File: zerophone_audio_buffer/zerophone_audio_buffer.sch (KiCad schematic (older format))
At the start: 7 parts, among them P1 CONN_01X03, P2 CONN_01X04, U1 LM1117-2.5, U2 NC7WZ16

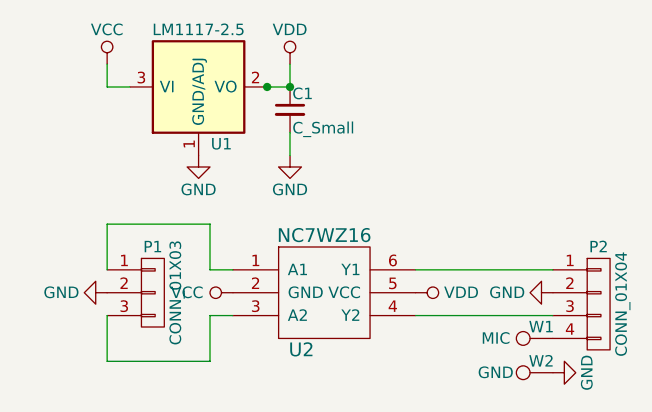
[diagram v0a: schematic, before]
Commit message: Corrected buffer pinout; changed power symbols
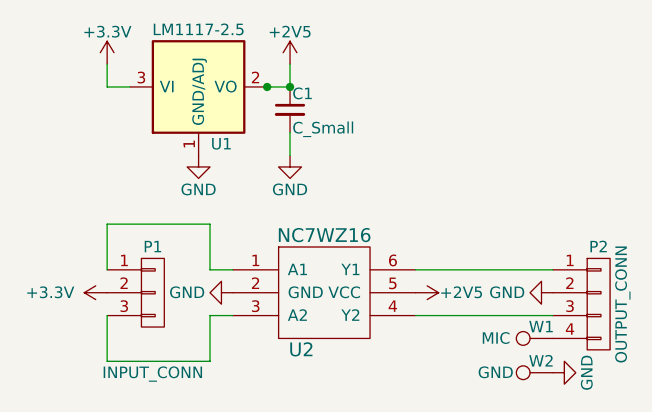
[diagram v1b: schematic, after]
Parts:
- P1: value CONN_01X03 -> INPUT_CONN
- P2: value CONN_01X04 -> OUTPUT_CONN
- W1, W2: footprint (none) -> Measurement_Points:Measurement_Point_Round-SMD-Pad_Small
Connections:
- net GND: now also U2.2 (GND); no longer P1.2 (P2)
- net VCC renamed +3V3
- net +3V3: now also P1.2 (P2); no longer U2.2 (GND)
- net VDD renamed +2V5
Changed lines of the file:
@@
 L GND #PWR01
 U 1 1 58BC7F11
-P 4850 2600
-F 0 "#PWR01" H 4850 2350 50  0001 C CNN
-F 1 "GND" V 4850 2400 50  0000 C CNN
-F 2 "" H 4850 2600 50  0000 C CNN
-F 3 "" H 4850 2600 50  0000 C CNN
-	1    4850 2600
-	0    1    1    0
-$EndComp
-$Comp
-L VDD #PWR02
-U 1 1 58BC7F41
-P 3700 1600
-F 0 "#PWR02" H 3700 1450 50  0001 C CNN
-F 1 "VDD" H 3700 1750 50  0000 C CNN
-F 2 "" H 3700 1600 50  0000 C CNN
-F 3 "" H 3700 1600 50  0000 C CNN
-	1    3700 1600
-	1    0    0    -1
-$EndComp
-$Comp
-L VCC #PWR03
-U 1 1 58BC7F5F
-P 2900 1600
-F 0 "#PWR03" H 2900 1450 50  0001 C CNN
-F 1 "VCC" H 2900 1750 50  0000 C CNN
-F 2 "" H 2900 1600 50  0000 C CNN
-F 3 "" H 2900 1600 50  0000 C CNN
-	1    2900 1600
-	1    0    0    -1
-$EndComp
-$Comp
-L VDD #PWR04
-U 1 1 58BC7F74
-P 4250 2600
-F 0 "#PWR04" H 4250 2450 50  0001 C CNN
-F 1 "VDD" V 4250 2800 50  0000 C CNN
-F 2 "" H 4250 2600 50  0000 C CNN
-F 3 "" H 4250 2600 50  0000 C CNN
-	1    4250 2600
+P 3450 2600
+F 0 "#PWR01" H 3450 2350 50  0001 C CNN
+F 1 "GND" V 3450 2400 50  0000 C CNN
+F 2 "" H 3450 2600 50  0000 C CNN
+F 3 "" H 3450 2600 50  0000 C CNN
+	1    3450 2600
 	0    1    1    0
 $EndComp
@@
 P 3100 2600
 F 0 "P1" H 3100 2800 50  0000 C CNN
-F 1 "CONN_01X03" V 3200 2600 50  0000 C CNN
+F 1 "INPUT_CONN" H 3100 2250 50  0000 C CNN
 F 2 "Pin_Headers:Pin_Header_Straight_1x03_Pitch2.54mm" H 3100 2600 50  0001 C CNN
 F 3 "" H 3100 2600 50  0000 C CNN
@@
 $EndComp
 $Comp
-L VCC #PWR05
-U 1 1 58BC7FEB
-P 3450 2600
-F 0 "#PWR05" H 3450 2450 50  0001 C CNN
-F 1 "VCC" V 3450 2800 50  0000 C CNN
-F 2 "" H 3450 2600 50  0000 C CNN
-F 3 "" H 3450 2600 50  0000 C CNN
-	1    3450 2600
-	0    -1   -1   0
-$EndComp
-$Comp
 L CONN_01X04 P2
 U 1 1 58BC80B3
 P 5050 2650
 F 0 "P2" H 5050 2900 50  0000 C CNN
-F 1 "CONN_01X04" V 5150 2650 50  0000 C CNN
+F 1 "OUTPUT_CONN" V 5150 2650 50  0000 C CNN
 F 2 "Pin_Headers:Pin_Header_Straight_1x04_Pitch2.54mm" H 5050 2650 50  0001 C CNN
 F 3 "" H 5050 2650 50  0000 C CNN
@@
 	4250 2700 4850 2700
 $Comp
-L GND #PWR06
+L GND #PWR02
 U 1 1 58BC8109
-P 2900 2600
-F 0 "#PWR06" H 2900 2350 50  0001 C CNN
-F 1 "GND" V 2900 2400 50  0000 C CNN
-F 2 "" H 2900 2600 50  0000 C CNN
-F 3 "" H 2900 2600 50  0000 C CNN
-	1    2900 2600
+P 4850 2600
+F 0 "#PWR02" H 4850 2350 50  0001 C CNN
+F 1 "GND" V 4850 2400 50  0000 C CNN
+F 2 "" H 4850 2600 50  0000 C CNN
+F 3 "" H 4850 2600 50  0000 C CNN
+	1    4850 2600
 	0    1    1    0
 $EndComp
@@
 	3700 1700 3600 1700
 $Comp
-L GND #PWR07
+L GND #PWR03
 U 1 1 58BC8213
 P 3300 2000
-F 0 "#PWR07" H 3300 1750 50  0001 C CNN
+F 0 "#PWR03" H 3300 1750 50  0001 C CNN
 F 1 "GND" H 3300 1850 50  0000 C CNN
 F 2 "" H 3300 2000 50  0000 C CNN
@@
 	3700 2000 3700 1900
 $Comp
-L GND #PWR08
+L GND #PWR04
 U 1 1 58BC84D9
 P 3700 2000
-F 0 "#PWR08" H 3700 1750 50  0001 C CNN
+F 0 "#PWR04" H 3700 1750 50  0001 C CNN
 F 1 "GND" H 3700 1850 50  0000 C CNN
 F 2 "" H 3700 2000 50  0000 C CNN
@@
 F 0 "W1" V 4900 2850 50  0000 C CNN
 F 1 "MIC" V 4850 3050 50  0000 C CNN
-F 2 "" H 5050 2800 50  0000 C CNN
+F 2 "Measurement_Points:Measurement_Point_Round-SMD-Pad_Small" H 5050 2800 50  0001 C CNN
 F 3 "" H 5050 2800 50  0000 C CNN
 	1    4850 2800
@@
 $EndComp
 $Comp
-L GND #PWR09
+L GND #PWR05
 U 1 1 58BC88F0
 P 4850 2950
-F 0 "#PWR09" H 4850 2700 50  0001 C CNN
+F 0 "#PWR05" H 4850 2700 50  0001 C CNN
 F 1 "GND" H 4850 2800 50  0000 C CNN
 F 2 "" H 4850 2950 50  0000 C CNN
@@
 F 0 "W2" V 4900 3000 50  0000 C CNN
 F 1 "GND" V 4850 3200 50  0000 C CNN
-F 2 "" H 5050 2950 50  0000 C CNN
+F 2 "Measurement_Points:Measurement_Point_Round-SMD-Pad_Small" H 5050 2950 50  0001 C CNN
 F 3 "" H 5050 2950 50  0000 C CNN
 	1    4850 2950
@@
 Wire Wire Line
 	3350 2700 3450 2700
+$Comp
+L +3.3V #PWR06
+U 1 1 58C39217
+P 2900 1600
+F 0 "#PWR06" H 2900 1450 50  0001 C CNN
+F 1 "+3.3V" H 2900 1740 50  0000 C CNN
+F 2 "" H 2900 1600 50  0000 C CNN
+F 3 "" H 2900 1600 50  0000 C CNN
+	1    2900 1600
+	1    0    0    -1
+$EndComp
+$Comp
+L +3.3V #PWR07
+U 1 1 58C3929D
+P 2900 2600
+F 0 "#PWR07" H 2900 2450 50  0001 C CNN
+F 1 "+3.3V" V 2900 2850 50  0000 C CNN
+F 2 "" H 2900 2600 50  0000 C CNN
+F 3 "" H 2900 2600 50  0000 C CNN
+	1    2900 2600
+	0    -1   -1   0
+$EndComp
+$Comp
+L +2V5 #PWR08
+U 1 1 58C392E1
+P 3700 1600
+F 0 "#PWR08" H 3700 1450 50  0001 C CNN
+F 1 "+2V5" H 3700 1740 50  0000 C CNN
+F 2 "" H 3700 1600 50  0000 C CNN
+F 3 "" H 3700 1600 50  0000 C CNN
+	1    3700 1600
+	1    0    0    -1
+$EndComp
+$Comp
+L +2V5 #PWR09
+U 1 1 58C3934E
+P 4250 2600
+F 0 "#PWR09" H 4250 2450 50  0001 C CNN
+F 1 "+2V5" V 4250 2800 50  0000 C CNN
+F 2 "" H 4250 2600 50  0000 C CNN
+F 3 "" H 4250 2600 50  0000 C CNN
+	1    4250 2600
+	0    1    1    0
+$EndComp
 $EndSCHEMATC
